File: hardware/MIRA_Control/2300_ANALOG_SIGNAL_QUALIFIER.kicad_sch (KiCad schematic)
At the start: 16 parts, among them U2300 TLV76033DBZR, U2301 TPS3808G01DBVR, U2302 SN74LVC1G11, U2303 74LVC1G17GV,125

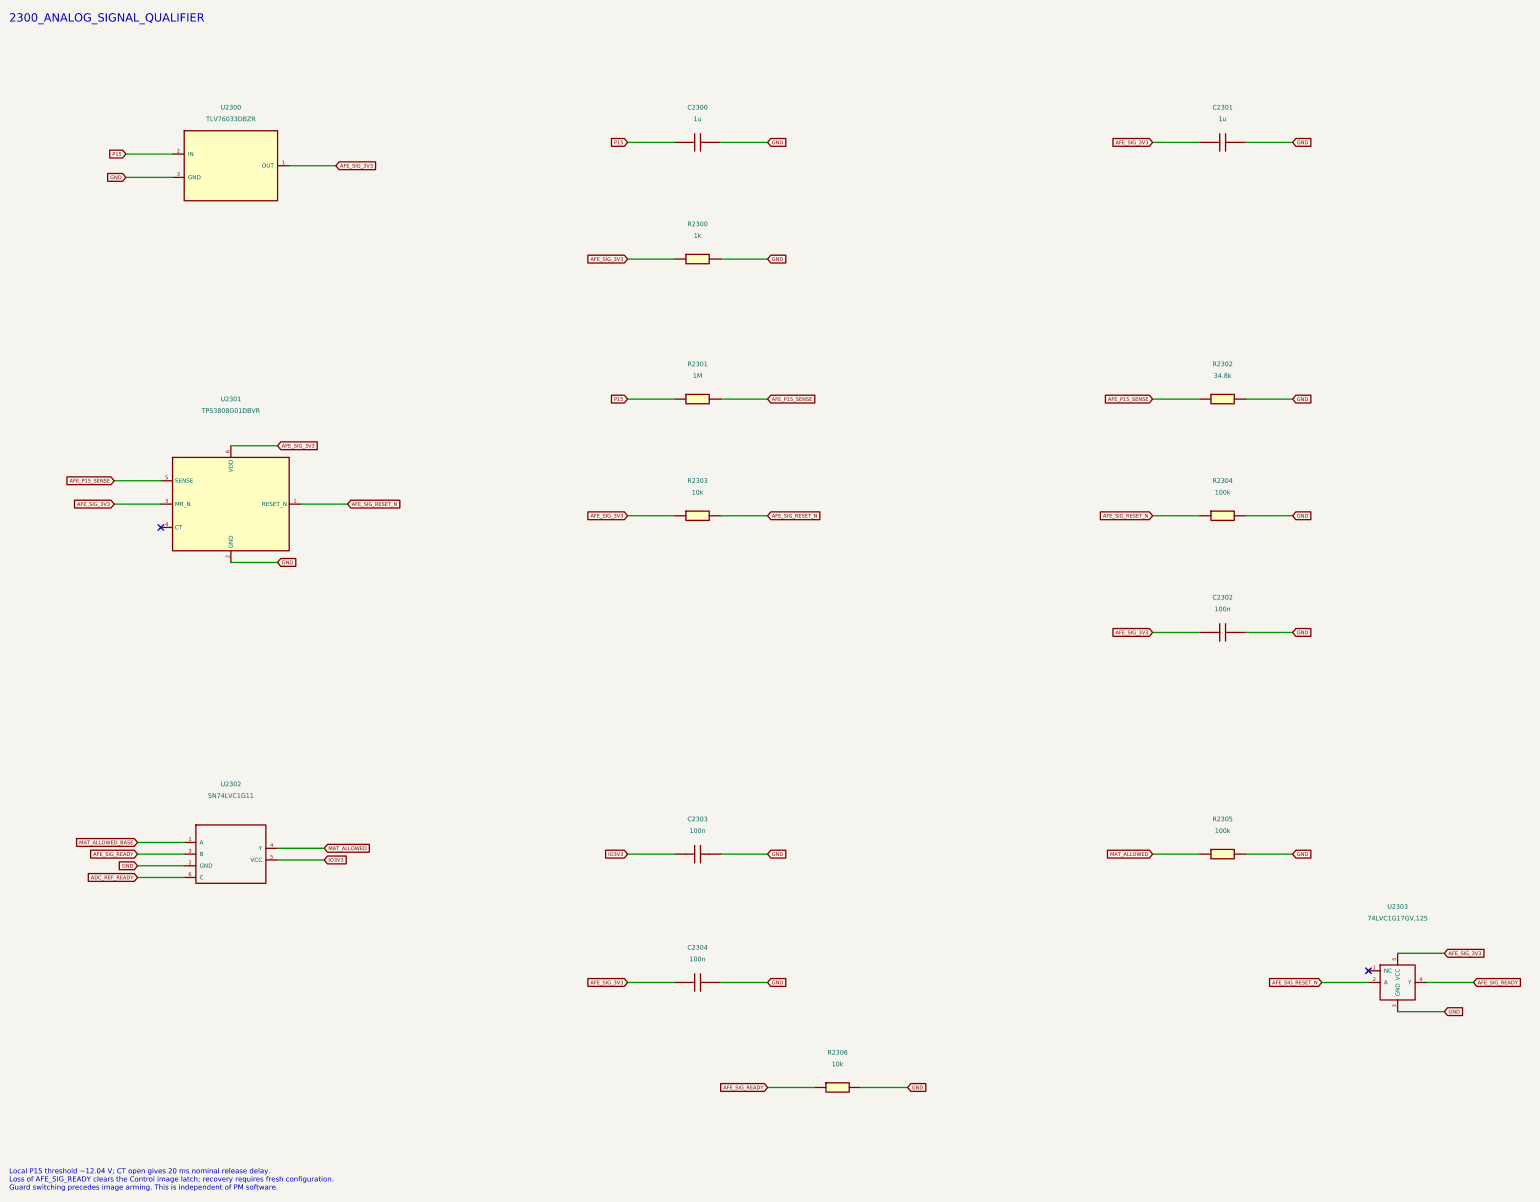
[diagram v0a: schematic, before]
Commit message: MIRA.05: analog requirements and schematic fixes
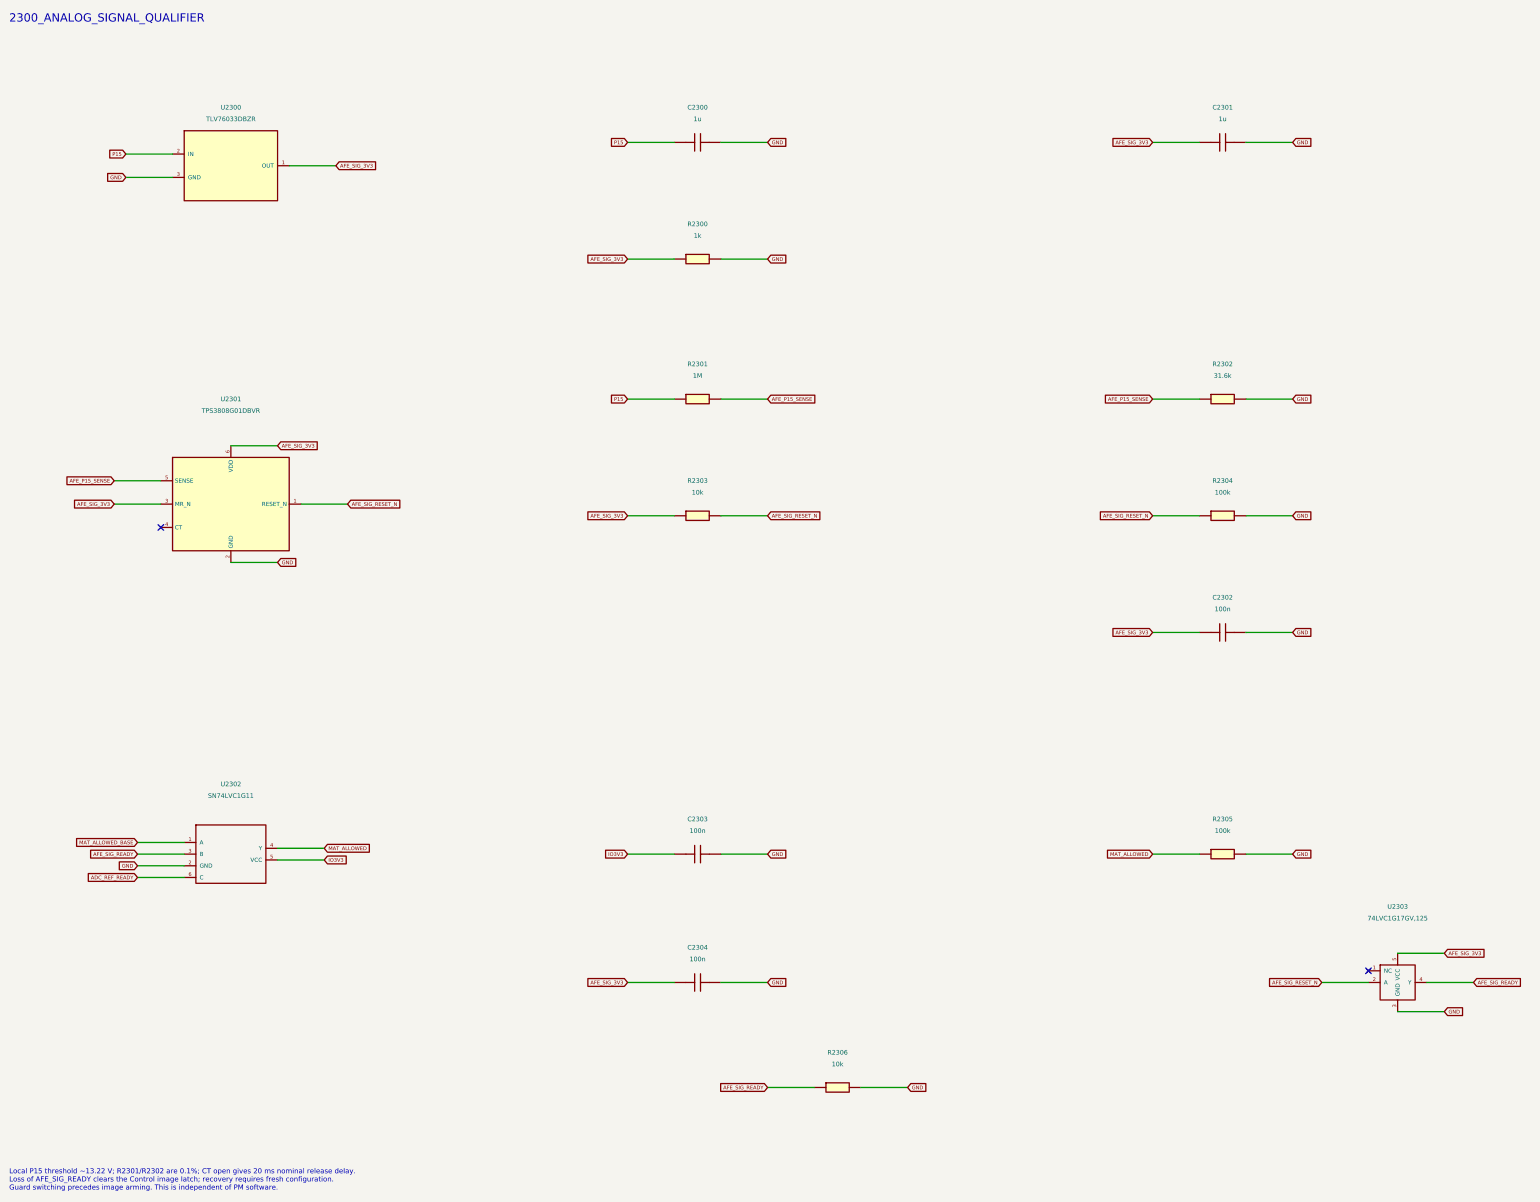
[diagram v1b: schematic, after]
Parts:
- R2301: footprint MIRA_RevA:R_0402_1005Metric -> MIRA_RevA:R_0603_1608Metric; MPN ERJ-2RKF1004X -> RT0603BRD071ML; Manufacturer Panasonic -> YAGEO
- R2302: value 34.8k -> 31.6k; footprint MIRA_RevA:R_0402_1005Metric -> MIRA_RevA:R_0603_1608Metric; MPN ERJ-2RKF3482X -> RT0603BRD0731K6L; Manufacturer Panasonic -> YAGEO
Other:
- note added: "Local P15 threshold ~13.22 V; R2301/R2302 are 0.1%; CT open gives 20 ms nominal release delay. Loss of AFE_SIG_READY clears the Control image latch; recovery requires fresh configuration. Guard switching precedes image arming. This is independent of PM software."
- note removed: "Local P15 threshold ~12.04 V; CT open gives 20 ms nominal release delay. Loss of AFE_SIG_READY clears the Control image latch; recovery requires fresh configuration. Guard switching precedes image arming. This is independent of PM software."
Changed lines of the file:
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@@
 (wire (pts (xy 170.18 96.52) (xy 180.34 96.52)) (stroke (width 0) (type default)))
 (global_label "AFE_P15_SENSE" (shape input) (at 180.34 96.52 0) (effects (font (size 0.8 0.8)) (justify left)))
-(symbol (lib_id "MIRA_RevA:SIG_R_1M") (at 165.1 96.52 0) (unit 1) (in_bom yes) (on_board yes) (dnp no) (property "Reference" "R2301" (at 165.1 88.89999999999999 0) (show_name no) (do_not_autoplace no) (effects (font (size 1 1)))) (property "Value" "1M" (at 165.1 91.44 0) (show_name no) (do_not_autoplace no) (effects (font (size 1 1)))) (property "Footprint" "MIRA_RevA:R_0402_1005Metric" (at 165.1 91.44 0) (show_name no) (do_not_autoplace no) (hide yes) (effects (font (size 1 1))) (hide yes)) (property "Datasheet" "" (at 165.1 91.44 0) (show_name no) (do_not_autoplace no) (hide yes) (effects (font (size 1 1))) (hide yes)) (property "Description" "Enable pulldown; default OFF" (at 165.1 91.44 0) (show_name no) (do_not_autoplace no) (hide yes) (effects (font (size 1 1))) (hide yes)) (property "MPN" "ERJ-2RKF1004X" (at 165.1 91.44 0) (show_name no) (do_not_autoplace no) (hide yes) (effects (font (size 1 1))) (hide yes)) (property "Manufacturer" "Panasonic" (at 165.1 91.44 0) (show_name no) (do_not_autoplace no) (hide yes) (effects (font (size 1 1))) (hide yes)) (pin "1") (pin "2") (instances (project "MIRA_Control" (path "/ad010b50-c509-466c-b833-d1667dfb0702/cfe91fde-fe4e-4fb2-ac7c-6adecfe1ecda" (reference "R2301") (unit 1)))))
+(symbol (lib_id "MIRA_RevA:SIG_R_1M") (at 165.1 96.52 0) (unit 1) (in_bom yes) (on_board yes) (dnp no) (property "Reference" "R2301" (at 165.1 88.89999999999999 0) (show_name no) (do_not_autoplace no) (effects (font (size 1 1)))) (property "Value" "1M" (at 165.1 91.44 0) (show_name no) (do_not_autoplace no) (effects (font (size 1 1)))) (property "Footprint" "MIRA_RevA:R_0603_1608Metric" (at 165.1 91.44 0) (show_name no) (do_not_autoplace no) (hide yes) (effects (font (size 1 1))) (hide yes)) (property "Datasheet" "https://www.yageogroup.com/component-documentation/download/specsheet/RT0603BRD071ML" (at 165.1 91.44 0) (show_name no) (do_not_autoplace no) (hide yes) (effects (font (size 1 1))) (hide yes)) (property "Description" "Precision resistor, 0.1%, 25 ppm/C; MIRA.05 analog operating envelope" (at 165.1 91.44 0) (show_name no) (do_not_autoplace no) (hide yes) (effects (font (size 1 1))) (hide yes)) (property "MPN" "RT0603BRD071ML" (at 165.1 91.44 0) (show_name no) (do_not_autoplace no) (hide yes) (effects (font (size 1 1))) (hide yes)) (property "Manufacturer" "YAGEO" (at 165.1 91.44 0) (show_name no) (do_not_autoplace no) (hide yes) (effects (font (size 1 1))) (hide yes)) (pin "1") (pin "2") (instances (project "MIRA_Control" (path "/ad010b50-c509-466c-b833-d1667dfb0702/cfe91fde-fe4e-4fb2-ac7c-6adecfe1ecda" (reference "R2301") (unit 1)))))
 (wire (pts (xy 274.32 96.52) (xy 264.16 96.52)) (stroke (width 0) (type default)))
 (global_label "AFE_P15_SENSE" (shape input) (at 264.16 96.52 180) (effects (font (size 0.8 0.8)) (justify right)))
 (wire (pts (xy 284.48 96.52) (xy 294.64 96.52)) (stroke (width 0) (type default)))
 (global_label "GND" (shape input) (at 294.64 96.52 0) (effects (font (size 0.8 0.8)) (justify left)))
-(symbol (lib_id "MIRA_RevA:SIG_R_34p8k") (at 279.4 96.52 0) (unit 1) (in_bom yes) (on_board yes) (dnp no) (property "Reference" "R2302" (at 279.4 88.89999999999999 0) (show_name no) (do_not_autoplace no) (effects (font (size 1 1)))) (property "Value" "34.8k" (at 279.4 91.44 0) (show_name no) (do_not_autoplace no) (effects (font (size 1 1)))) (property "Footprint" "MIRA_RevA:R_0402_1005Metric" (at 279.4 91.44 0) (show_name no) (do_not_autoplace no) (hide yes) (effects (font (size 1 1))) (hide yes)) (property "Datasheet" "" (at 279.4 91.44 0) (show_name no) (do_not_autoplace no) (hide yes) (effects (font (size 1 1))) (hide yes)) (property "Description" "Enable pulldown; default OFF" (at 279.4 91.44 0) (show_name no) (do_not_autoplace no) (hide yes) (effects (font (size 1 1))) (hide yes)) (property "MPN" "ERJ-2RKF3482X" (at 279.4 91.44 0) (show_name no) (do_not_autoplace no) (hide yes) (effects (font (size 1 1))) (hide yes)) (property "Manufacturer" "Panasonic" (at 279.4 91.44 0) (show_name no) (do_not_autoplace no) (hide yes) (effects (font (size 1 1))) (hide yes)) (pin "1") (pin "2") (instances (project "MIRA_Control" (path "/ad010b50-c509-466c-b833-d1667dfb0702/cfe91fde-fe4e-4fb2-ac7c-6adecfe1ecda" (reference "R2302") (unit 1)))))
+(symbol (lib_id "MIRA_RevA:SIG_R_34p8k") (at 279.4 96.52 0) (unit 1) (in_bom yes) (on_board yes) (dnp no) (property "Reference" "R2302" (at 279.4 88.89999999999999 0) (show_name no) (do_not_autoplace no) (effects (font (size 1 1)))) (property "Value" "31.6k" (at 279.4 91.44 0) (show_name no) (do_not_autoplace no) (effects (font (size 1 1)))) (property "Footprint" "MIRA_RevA:R_0603_1608Metric" (at 279.4 91.44 0) (show_name no) (do_not_autoplace no) (hide yes) (effects (font (size 1 1))) (hide yes)) (property "Datasheet" "https://www.yageogroup.com/component-documentation/download/specsheet/RT0603BRD0731K6L" (at 279.4 91.44 0) (show_name no) (do_not_autoplace no) (hide yes) (effects (font (size 1 1))) (hide yes)) (property "Description" "Precision resistor, 0.1%, 25 ppm/C; MIRA.05 analog operating envelope" (at 279.4 91.44 0) (show_name no) (do_not_autoplace no) (hide yes) (effects (font (size 1 1))) (hide yes)) (property "MPN" "RT0603BRD0731K6L" (at 279.4 91.44 0) (show_name no) (do_not_autoplace no) (hide yes) (effects (font (size 1 1))) (hide yes)) (property "Manufacturer" "YAGEO" (at 279.4 91.44 0) (show_name no) (do_not_autoplace no) (hide yes) (effects (font (size 1 1))) (hide yes)) (pin "1") (pin "2") (instances (project "MIRA_Control" (path "/ad010b50-c509-466c-b833-d1667dfb0702/cfe91fde-fe4e-4fb2-ac7c-6adecfe1ecda" (reference "R2302") (unit 1)))))
 (wire (pts (xy 160.02 121.92) (xy 149.86 121.92)) (stroke (width 0) (type default)))
 (global_label "AFE_SIG_3V3" (shape input) (at 149.86 121.92 180) (effects (font (size 0.8 0.8)) (justify right)))
@@
 (global_label "GND" (shape input) (at 210.82 246.38 0) (effects (font (size 0.8 0.8)) (justify left)))
 (symbol (lib_id "MIRA_RevA:SIG_R_10k") (at 195.58 246.38 0) (unit 1) (in_bom yes) (on_board yes) (dnp no) (property "Reference" "R2306" (at 195.58 238.76 0) (show_name no) (do_not_autoplace no) (effects (font (size 1 1)))) (property "Value" "10k" (at 195.58 241.29999999999998 0) (show_name no) (do_not_autoplace no) (effects (font (size 1 1)))) (property "Footprint" "MIRA_RevA:R_0402_1005Metric" (at 195.58 241.29999999999998 0) (show_name no) (do_not_autoplace no) (hide yes) (effects (font (size 1 1))) (hide yes)) (property "Datasheet" "" (at 195.58 241.29999999999998 0) (show_name no) (do_not_autoplace no) (hide yes) (effects (font (size 1 1))) (hide yes)) (property "Description" "Enable pulldown; default OFF" (at 195.58 241.29999999999998 0) (show_name no) (do_not_autoplace no) (hide yes) (effects (font (size 1 1))) (hide yes)) (property "MPN" "ERJ-2RKF1002X" (at 195.58 241.29999999999998 0) (show_name no) (do_not_autoplace no) (hide yes) (effects (font (size 1 1))) (hide yes)) (property "Manufacturer" "Panasonic" (at 195.58 241.29999999999998 0) (show_name no) (do_not_autoplace no) (hide yes) (effects (font (size 1 1))) (hide yes)) (pin "1") (pin "2") (instances (project "MIRA_Control" (path "/ad010b50-c509-466c-b833-d1667dfb0702/cfe91fde-fe4e-4fb2-ac7c-6adecfe1ecda" (reference "R2306") (unit 1)))))
-(text "Local P15 threshold ~12.04 V; CT open gives 20 ms nominal release delay.\nLoss of AFE_SIG_READY clears the Control image latch; recovery requires fresh configuration.\nGuard switching precedes image arming. This is independent of PM software." (at 15.24 264.16 0) (effects (font (size 1.1 1.1)) (justify left top)))
+(text "Local P15 threshold ~13.22 V; R2301/R2302 are 0.1%; CT open gives 20 ms nominal release delay.\nLoss of AFE_SIG_READY clears the Control image latch; recovery requires fresh configuration.\nGuard switching precedes image arming. This is independent of PM software." (at 15.24 264.16 0) (effects (font (size 1.1 1.1)) (justify left top)))
 (embedded_fonts no)
 (wire (pts (xy 53.34 193.04) (xy 43.18 193.04)) (stroke (width 0) (type default)))
